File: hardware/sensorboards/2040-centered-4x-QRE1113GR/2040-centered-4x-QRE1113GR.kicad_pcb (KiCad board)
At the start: 2 copper layers, 47.5 x 45 mm, 14 parts, among them J1 Conn_01x10_Male, U1 QRE1113GR, U2 QRE1113GR, U3 QRE1113GR, U4 QRE1113GR

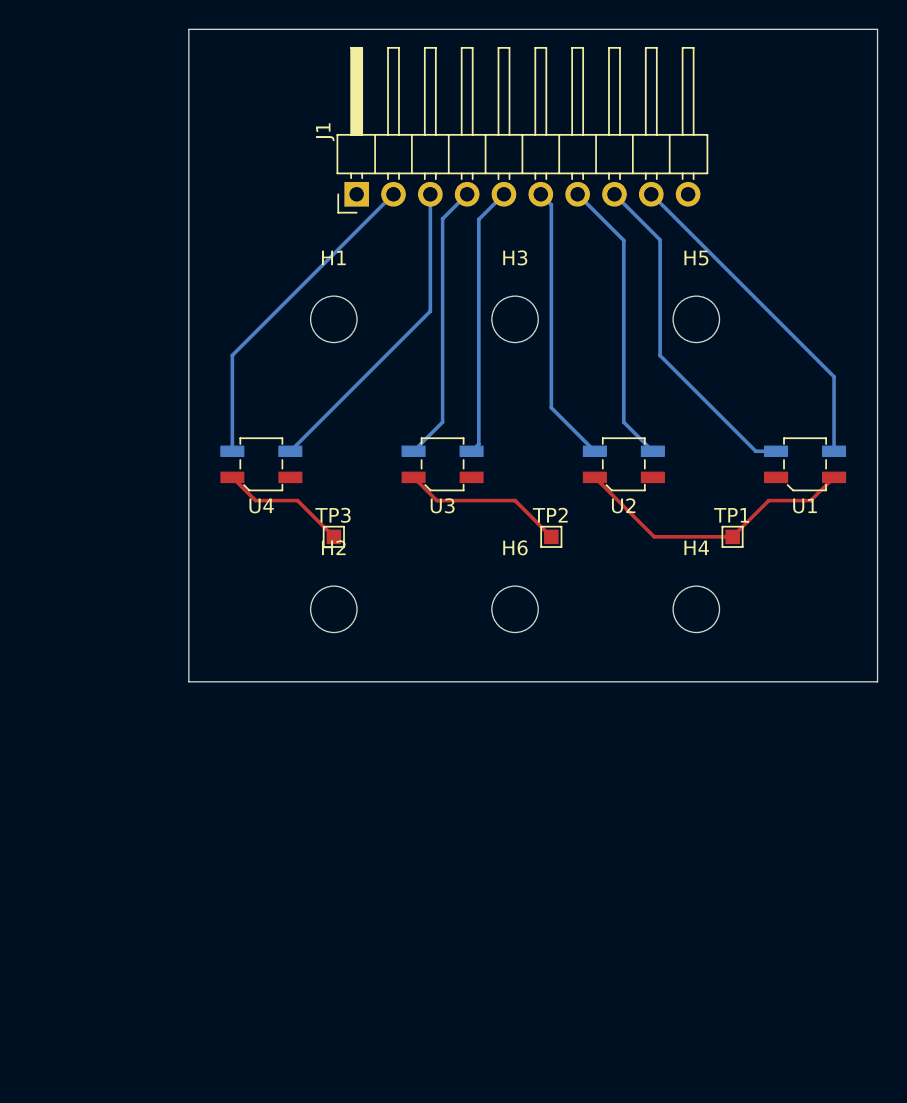
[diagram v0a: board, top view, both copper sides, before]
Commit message: Changing the connector pins to accommodate easier PCB layout
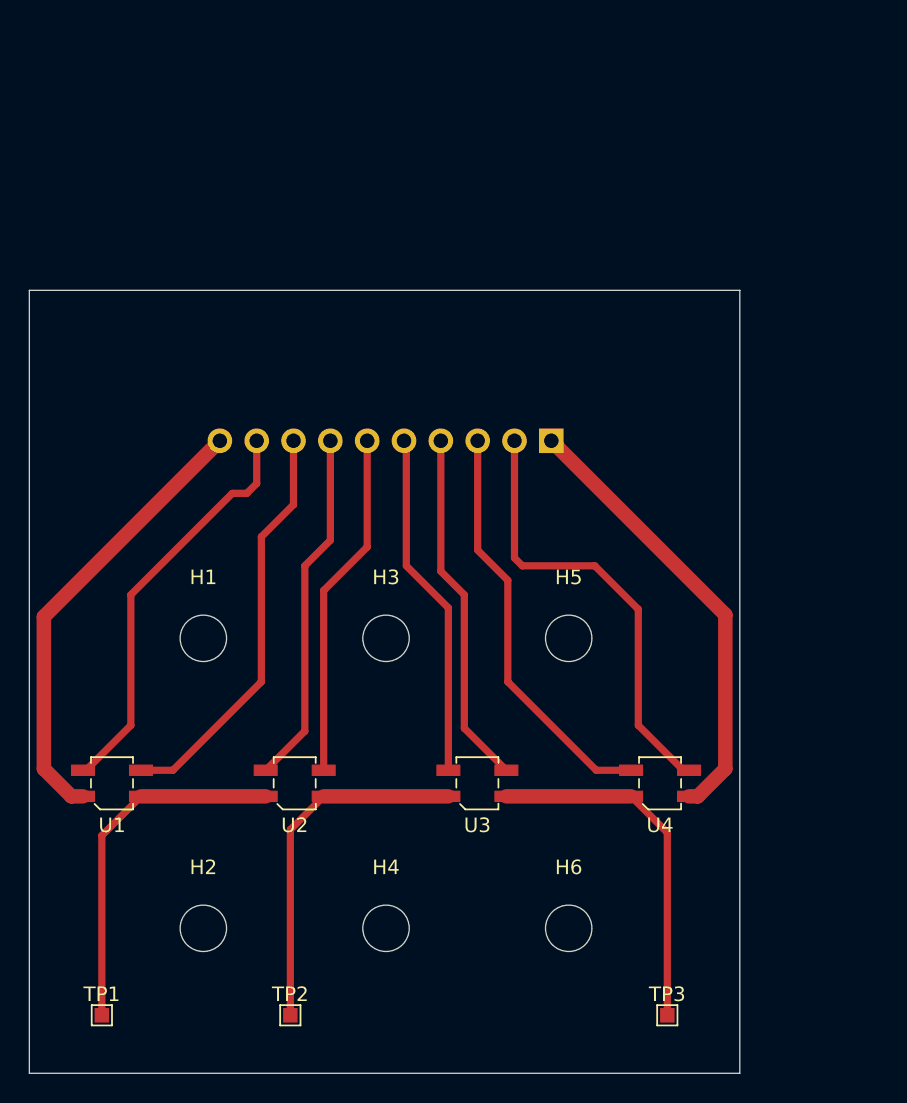
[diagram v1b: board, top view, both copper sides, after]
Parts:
- J1: moved to B.Cu
- moved TP1 54.6 mm to (119.0, 108.0)
- moved U1 52.6 mm to (119.7, 92.0)
- moved TP3 40.2 mm to (158.0, 108.0)
- moved TP2 37.6 mm to (132.0, 108.0)
- moved U4 35.2 mm to (157.5, 92.0)
- moved U2 31.6 mm to (132.3, 92.0)
- moved H4 30.7 mm to (138.6, 102.0)
- moved H1 23.8 mm to (126.0, 82.0)
- moved H2 23.8 mm to (126.0, 102.0)
- moved H3 23.7 mm to (138.6, 82.0)
- moved H5 23.7 mm to (151.2, 82.0)
- moved H6 22.3 mm to (151.2, 102.0)
- moved U3 22.1 mm to (144.9, 92.0)
- moved J1 21.7 mm to (150.0, 68.4)
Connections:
- J1 pad 2: /E4 -> /C4
- J1 pad 3: /C4 -> /E4
- J1 pad 4: /E3 -> /C3
- J1 pad 5: /C3 -> /E3
- J1 pad 6: /E2 -> Net-(J1-Pad6)
- J1 pad 7: /C2 -> /E2
- J1 pad 8: /E1 -> /C1
- J1 pad 9: /C1 -> /E1
- U2 pad 3: /C2 -> Net-(J1-Pad6)
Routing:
- net /POS: track 0.00 -> 31.1 mm
- net /NEG: track 0.57 -> 30.9 mm
- net Net-(J1-Pad6): track 0.00 -> 24.0 mm
- net /C2: track 19.9 -> 0.00 mm
- net Net-(TP3-Pad1): track 8.70 -> 24.7 mm
- net Net-(TP2-Pad1): track 11.2 -> 24.7 mm
- net /C4: track 21.7 -> 30.9 mm
- net /E4: track 22.3 -> 28.5 mm
- net /C3: track 18.7 -> 24.6 mm
- net /C1: track 23.0 -> 28.4 mm
- net /E2: track 19.3 -> 24.6 mm
- net /E1: track 23.2 -> 28.4 mm
- net Net-(TP1-Pad1): track 19.9 -> 24.8 mm
- net /E3: track 19.3 -> 24.0 mm
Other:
- board size 47.5 x 45 mm -> 49 x 54 mm

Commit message: - using straight, rather than angled, connector - adjusted the board size - included 3D models - added a README and a raytracing model of the board
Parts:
- added ?: , , F.Cu at (168.1, 92.1)
- J1: footprint Pin_Headers:Pin_Header_Angled_1x10_Pitch2.54mm -> Connector_PinHeader_2.54mm:PinHeader_1x10_P2.54mm_Vertical
- moved J1 0.08 mm to (150.0, 68.3)
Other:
- board size 49 x 54 mm -> 49 x 46.5 mm

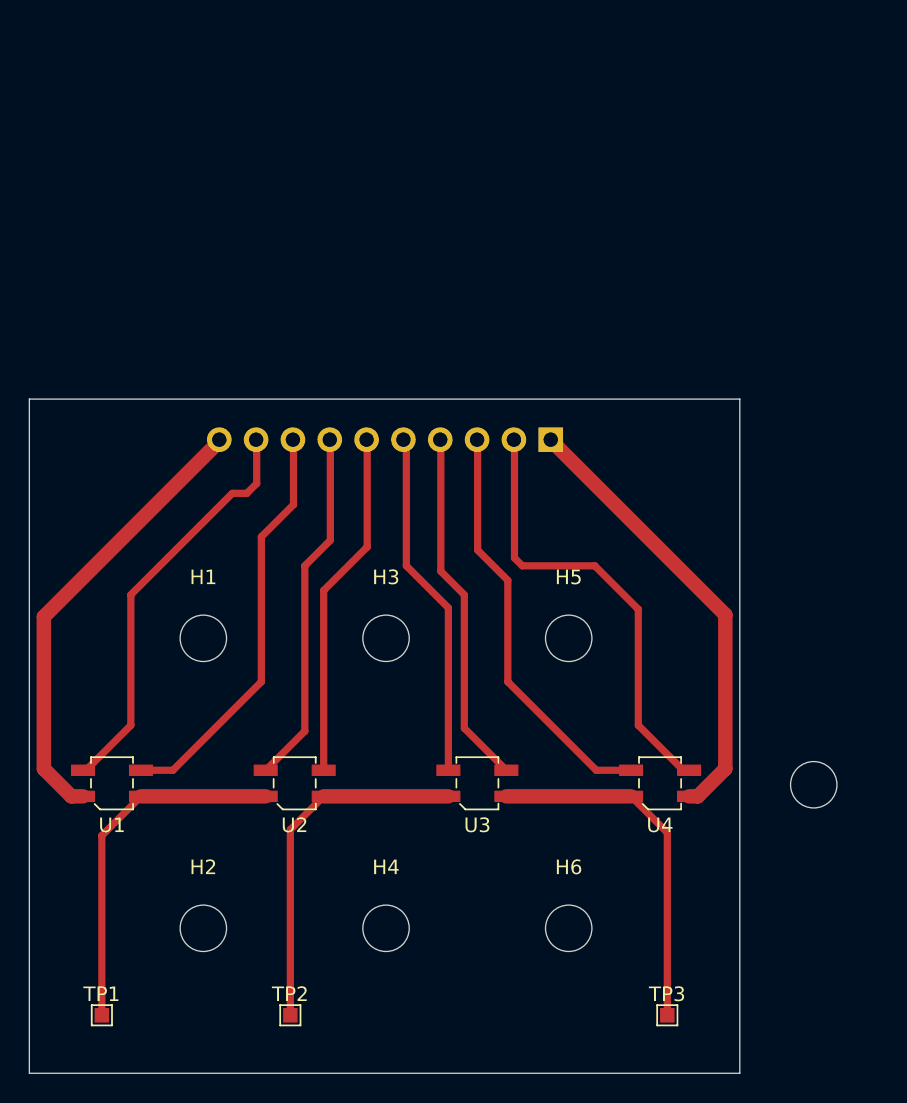
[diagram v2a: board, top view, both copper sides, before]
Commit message: implementing comments from https://pianoclack.com/forum/d/542-update-on-piano-conversion/12
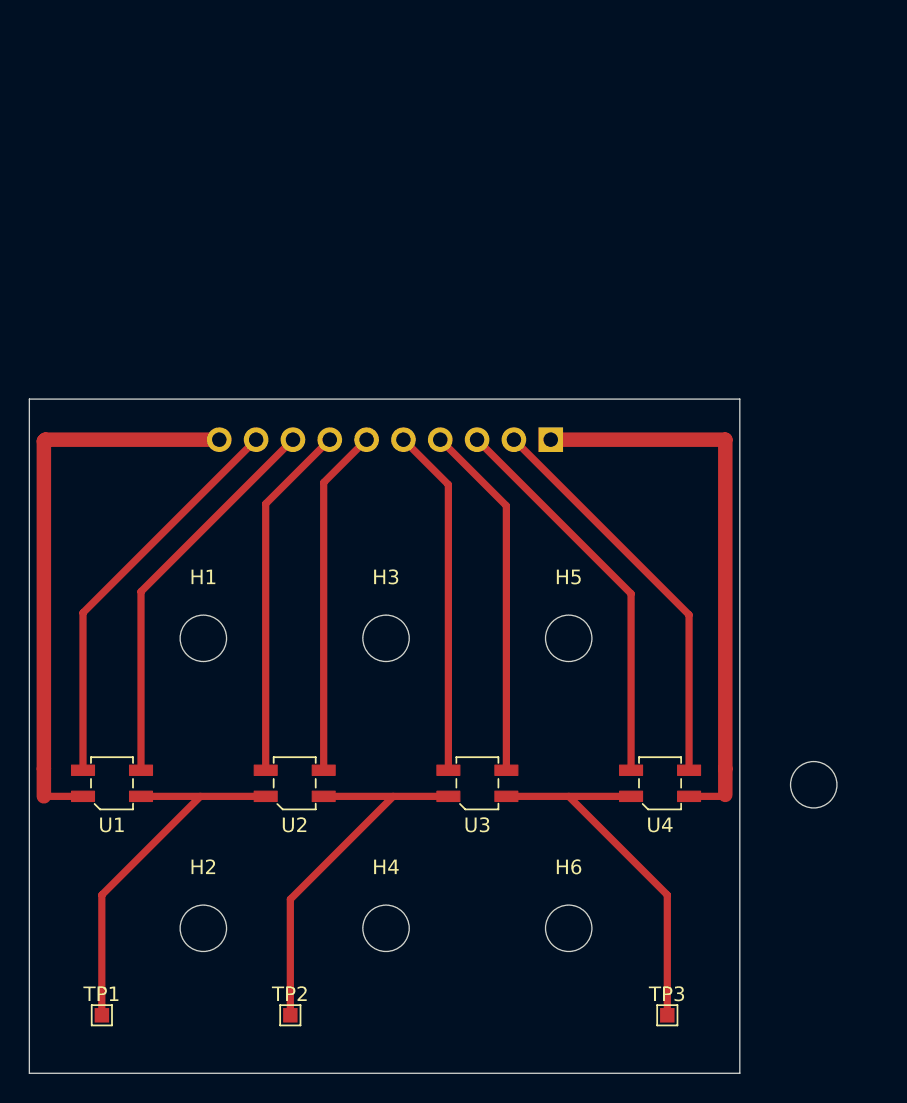
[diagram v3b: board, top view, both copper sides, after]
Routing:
- net /POS: track 31.1 -> 39.3 mm
- net /NEG: track 30.9 -> 39.1 mm
- net /C4: track 30.9 -> 28.2 mm
- net Net-(TP2-Pad1): track 24.7 -> 26.6 mm
- net Net-(TP3-Pad1): track 24.7 -> 26.5 mm
- net Net-(TP1-Pad1): track 24.8 -> 26.5 mm
- net /E4: track 28.5 -> 27.2 mm
- net /C1: track 28.4 -> 27.1 mm
- net /E1: track 28.4 -> 27.7 mm
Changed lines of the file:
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@@
   )
   (gr_rect (start 114 65.5) (end 163 112) (layer "Edge.Cuts") (width 0.05) (fill none))
-  (segment (start 162 91) (end 162 80.375) (width 1) (layer "F.Cu") (net 1))
-  (segment (start 159.5 92.9) (end 160.1 92.9) (width 1) (layer "F.Cu") (net 1))
-  (segment (start 162 80.375) (end 150 68.375) (width 1) (layer "F.Cu") (net 1))
-  (segment (start 160.1 92.9) (end 162 91) (width 1) (layer "F.Cu") (net 1))
-  (segment (start 147 85) (end 147 78) (width 0.5) (layer "F.Cu") (net 2))
-  (segment (start 155.5 91.1) (end 153.1 91.1) (width 0.5) (layer "F.Cu") (net 2))
-  (segment (start 144.92 75.92) (end 144.92 68.375) (width 0.5) (layer "F.Cu") (net 2))
-  (segment (start 147 78) (end 144.92 75.92) (width 0.5) (layer "F.Cu") (net 2))
-  (segment (start 153.1 91.1) (end 147 85) (width 0.5) (layer "F.Cu") (net 2))
-  (segment (start 159.1 91.1) (end 156 88) (width 0.5) (layer "F.Cu") (net 3))
+  (segment (start 149.96 68.3) (end 162 68.3) (width 1) (layer "F.Cu") (net 1))
+  (segment (start 162 68.3) (end 162 91) (width 1) (layer "F.Cu") (net 1))
+  (segment (start 162 91) (end 162 92.8) (width 1) (layer "F.Cu") (net 1))
+  (segment (start 159.5 92.9) (end 161.9 92.9) (width 0.5) (layer "F.Cu") (net 1))
+  (segment (start 161.9 92.9) (end 162 92.8) (width 0.5) (layer "F.Cu") (net 1))
+  (segment (start 155.5 78.92) (end 155.5 91.1) (width 0.5) (layer "F.Cu") (net 2))
+  (segment (start 144.88 68.3) (end 155.5 78.92) (width 0.5) (layer "F.Cu") (net 2))
+  (segment (start 159.5 80.38) (end 147.42 68.3) (width 0.5) (layer "F.Cu") (net 3))
+  (segment (start 159.5 91.1) (end 159.5 80.38) (width 0.5) (layer "F.Cu") (net 3))
   (segment (start 159.5 91.1) (end 159.1 91.1) (width 0.5) (layer "F.Cu") (net 3))
-  (segment (start 148 77) (end 147.46 76.46) (width 0.5) (layer "F.Cu") (net 3))
-  (segment (start 147.46 76.46) (end 147.46 68.375) (width 0.5) (layer "F.Cu") (net 3))
-  (segment (start 156 88) (end 156 80) (width 0.5) (layer "F.Cu") (net 3))
-  (segment (start 156 80) (end 153 77) (width 0.5) (layer "F.Cu") (net 3))
-  (segment (start 153 77) (end 148 77) (width 0.5) (layer "F.Cu") (net 3))
-  (segment (start 140 77) (end 140 68.535) (width 0.5) (layer "F.Cu") (net 4))
-  (segment (start 142.9 91.1) (end 142.9 79.9) (width 0.5) (layer "F.Cu") (net 4))
-  (segment (start 142.9 79.9) (end 140 77) (width 0.5) (layer "F.Cu") (net 4))
+  (segment (start 142.9 71.4) (end 142.9 91.1) (width 0.5) (layer "F.Cu") (net 4))
+  (segment (start 139.8 68.3) (end 142.9 71.4) (width 0.5) (layer "F.Cu") (net 4))
   (segment (start 140 68.535) (end 139.84 68.375) (width 0.5) (layer "F.Cu") (net 4))
-  (segment (start 144 88.2) (end 144 79) (width 0.5) (layer "F.Cu") (net 5))
-  (segment (start 144 79) (end 142.38 77.38) (width 0.5) (layer "F.Cu") (net 5))
-  (segment (start 146.9 91.1) (end 144 88.2) (width 0.5) (layer "F.Cu") (net 5))
-  (segment (start 142.38 77.38) (end 142.38 68.375) (width 0.5) (layer "F.Cu") (net 5))
-  (segment (start 130.3 91.1) (end 133 88.4) (width 0.5) (layer "F.Cu") (net 6))
-  (segment (start 134.76 75.24) (end 134.76 68.375) (width 0.5) (layer "F.Cu") (net 6))
-  (segment (start 133 88.4) (end 133 77) (width 0.5) (layer "F.Cu") (net 6))
-  (segment (start 133 77) (end 134.76 75.24) (width 0.5) (layer "F.Cu") (net 6))
-  (segment (start 121 88) (end 121 79) (width 0.5) (layer "F.Cu") (net 7))
-  (segment (start 121 79) (end 128 72) (width 0.5) (layer "F.Cu") (net 7))
-  (segment (start 128 72) (end 129 72) (width 0.5) (layer "F.Cu") (net 7))
-  (segment (start 117.7 91.1) (end 117.9 91.1) (width 0.5) (layer "F.Cu") (net 7))
-  (segment (start 117.9 91.1) (end 121 88) (width 0.5) (layer "F.Cu") (net 7))
-  (segment (start 129 72) (end 129.68 71.32) (width 0.5) (layer "F.Cu") (net 7))
-  (segment (start 129.68 71.32) (end 129.68 68.375) (width 0.5) (layer "F.Cu") (net 7))
-  (segment (start 130 85) (end 130 75) (width 0.5) (layer "F.Cu") (net 8))
-  (segment (start 123.9 91.1) (end 130 85) (width 0.5) (layer "F.Cu") (net 8))
-  (segment (start 130 75) (end 132.22 72.78) (width 0.5) (layer "F.Cu") (net 8))
-  (segment (start 121.7 91.1) (end 123.9 91.1) (width 0.5) (layer "F.Cu") (net 8))
-  (segment (start 132.22 72.78) (end 132.22 68.375) (width 0.5) (layer "F.Cu") (net 8))
-  (segment (start 115 80.515) (end 127.14 68.375) (width 1) (layer "F.Cu") (net 9))
-  (segment (start 116.9 92.9) (end 115 91) (width 1) (layer "F.Cu") (net 9))
-  (segment (start 115 91) (end 115 80.515) (width 1) (layer "F.Cu") (net 9))
-  (segment (start 117.7 92.9) (end 116.9 92.9) (width 1) (layer "F.Cu") (net 9))
-  (segment (start 119 95.6) (end 119 108) (width 0.5) (layer "F.Cu") (net 10))
-  (segment (start 130.3 92.9) (end 121.7 92.9) (width 1) (layer "F.Cu") (net 10))
-  (segment (start 121.7 92.9) (end 119 95.6) (width 0.5) (layer "F.Cu") (net 10))
-  (segment (start 142.9 92.9) (end 134.3 92.9) (width 1) (layer "F.Cu") (net 11))
-  (segment (start 134.3 92.9) (end 132 95.2) (width 0.5) (layer "F.Cu") (net 11))
-  (segment (start 132 95.2) (end 132 108) (width 0.5) (layer "F.Cu") (net 11))
-  (segment (start 155.5 92.9) (end 158 95.4) (width 0.5) (layer "F.Cu") (net 12))
-  (segment (start 158 95.4) (end 158 108) (width 0.5) (layer "F.Cu") (net 12))
-  (segment (start 155.5 92.9) (end 146.9 92.9) (width 1) (layer "F.Cu") (net 12))
-  (segment (start 137.3 75.7) (end 137.3 68.375) (width 0.5) (layer "F.Cu") (net 13))
-  (segment (start 134.3 78.7) (end 137.3 75.7) (width 0.5) (layer "F.Cu") (net 13))
-  (segment (start 134.3 91.1) (end 134.3 78.7) (width 0.5) (layer "F.Cu") (net 13))
+  (segment (start 146.9 72.86) (end 146.9 91.1) (width 0.5) (layer "F.Cu") (net 5))
+  (segment (start 142.34 68.3) (end 146.9 72.86) (width 0.5) (layer "F.Cu") (net 5))
+  (segment (start 130.3 72.72) (end 130.3 91.1) (width 0.5) (layer "F.Cu") (net 6))
+  (segment (start 134.72 68.3) (end 130.3 72.72) (width 0.5) (layer "F.Cu") (net 6))
+  (segment (start 117.7 80.24) (end 129.64 68.3) (width 0.5) (layer "F.Cu") (net 7))
+  (segment (start 117.7 91.1) (end 117.7 80.24) (width 0.5) (layer "F.Cu") (net 7))
+  (segment (start 121.7 78.78) (end 121.7 91.1) (width 0.5) (layer "F.Cu") (net 8))
+  (segment (start 132.18 68.3) (end 121.7 78.78) (width 0.5) (layer "F.Cu") (net 8))
+  (segment (start 115 92.9) (end 117.7 92.9) (width 0.5) (layer "F.Cu") (net 9))
+  (segment (start 115.1 68.3) (end 127.1 68.3) (width 1) (layer "F.Cu") (net 9))
+  (segment (start 115 68.4) (end 115.1 68.3) (width 1) (layer "F.Cu") (net 9))
+  (segment (start 115 91) (end 115 92.9) (width 1) (layer "F.Cu") (net 9))
+  (segment (start 115 91) (end 115 68.4) (width 1) (layer "F.Cu") (net 9))
+  (segment (start 119 108) (end 119 99.7) (width 0.5) (layer "F.Cu") (net 10))
+  (segment (start 119 99.7) (end 125.8 92.9) (width 0.5) (layer "F.Cu") (net 10))
+  (segment (start 121.7 92.9) (end 130.3 92.9) (width 0.5) (layer "F.Cu") (net 10))
+  (segment (start 132 100) (end 139.1 92.9) (width 0.5) (layer "F.Cu") (net 11))
+  (segment (start 132 108) (end 132 100) (width 0.5) (layer "F.Cu") (net 11))
+  (segment (start 134.3 92.9) (end 142.9 92.9) (width 0.5) (layer "F.Cu") (net 11))
+  (segment (start 158 108) (end 158 99.7) (width 0.5) (layer "F.Cu") (net 12))
+  (segment (start 146.9 92.9) (end 155.5 92.9) (width 0.5) (layer "F.Cu") (net 12))
+  (segment (start 158 99.7) (end 151.2 92.9) (width 0.5) (layer "F.Cu") (net 12))
+  (segment (start 137.26 68.3) (end 134.3 71.26) (width 0.5) (layer "F.Cu") (net 13))
+  (segment (start 134.3 71.26) (end 134.3 91.1) (width 0.5) (layer "F.Cu") (net 13))
 )
